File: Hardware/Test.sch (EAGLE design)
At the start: 57 parts, among them IC1 4051N, IC2 TLC5940, IC3 MEGA8-P, T1 BC548, T2 BC548, T3 BC548, T4 BC548, T5 BC548, T6 BC548, T8 BC548, T9 BC548

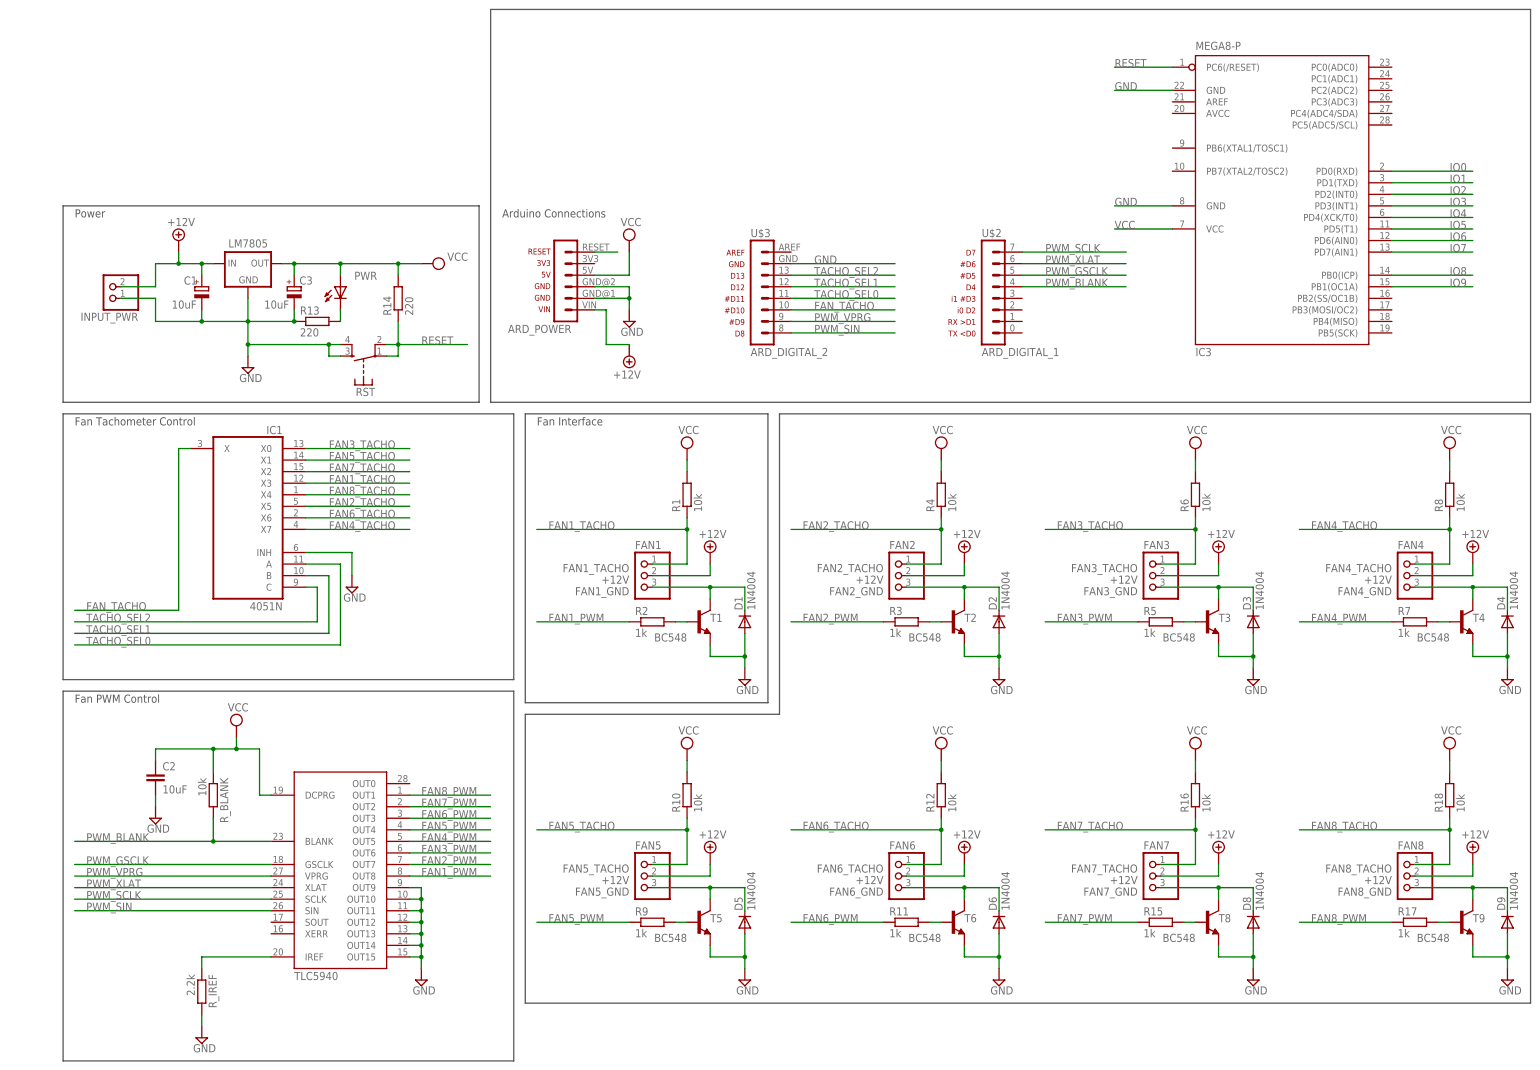
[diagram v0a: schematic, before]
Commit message: Added some test schematics
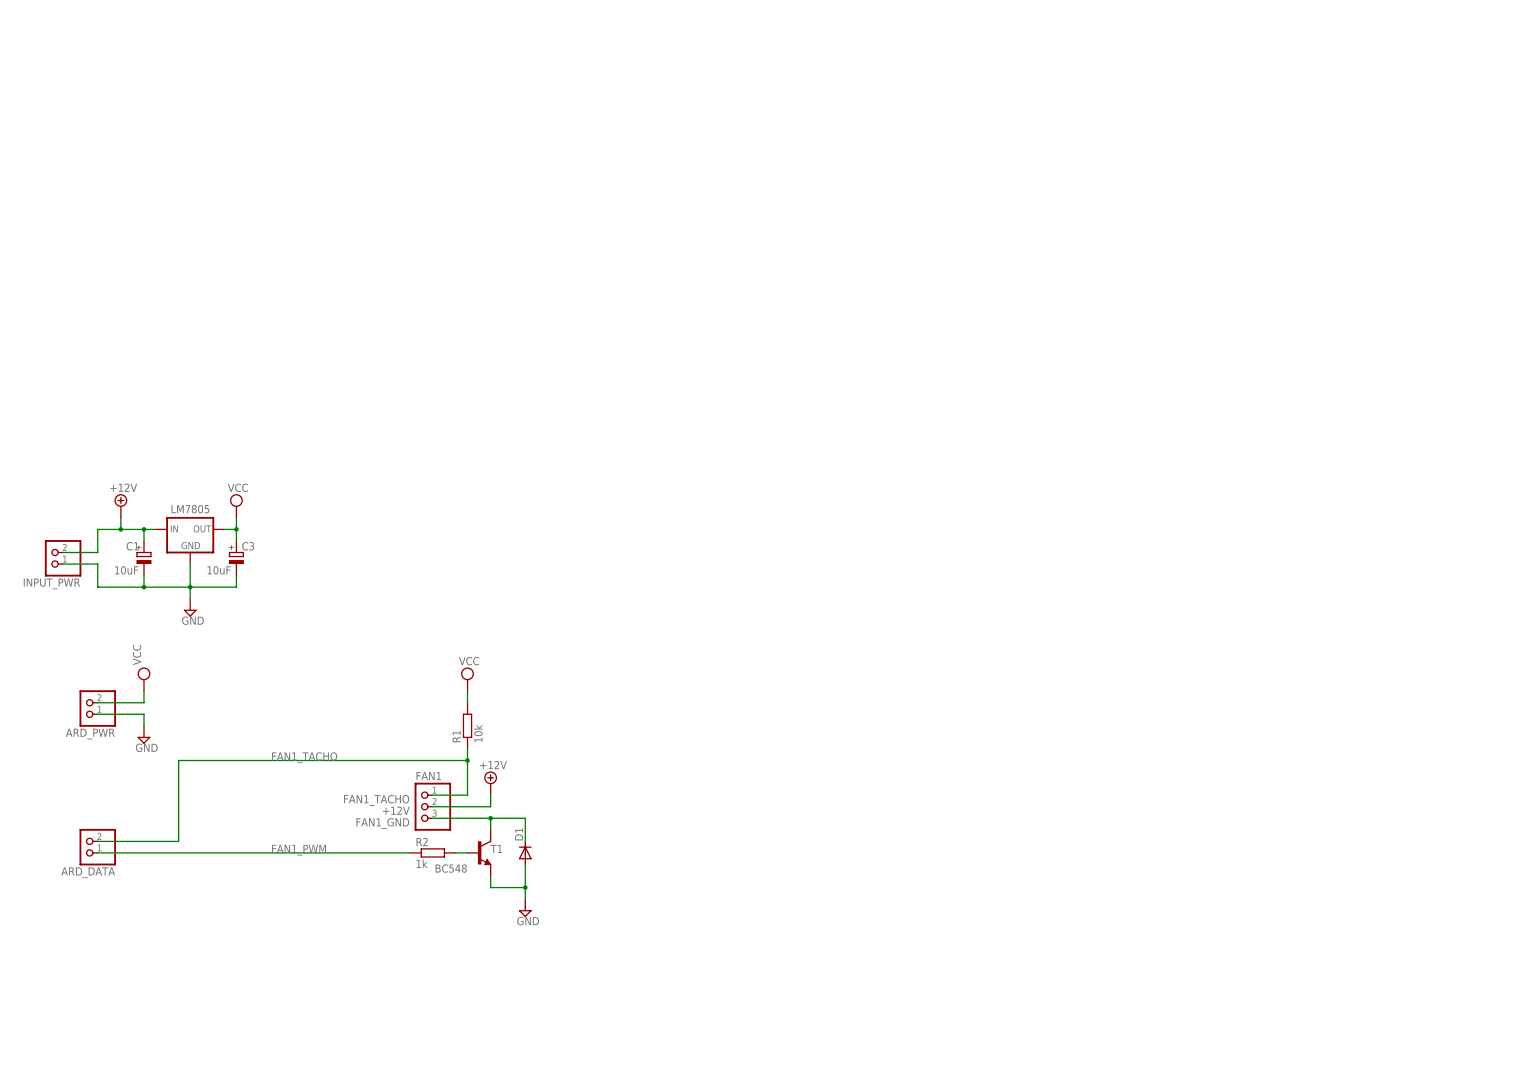
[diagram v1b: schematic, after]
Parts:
- removed C2: 10uF, rcl:C-EU025-025X050
- removed D2, D3, D4, D5, D6, D8, D9: 1N4004, diode:1N4004
- removed FAN2, FAN3, FAN4, FAN5, FAN6, FAN7, FAN8: (no value), pinhead:PINHD-1X3
- removed IC1: 4051N, 40xx:4051N
- removed IC2: TLC5940, EnigmaMon:TLC5940
- removed IC3: MEGA8-P, EnigmaMon:MEGA8-P
- removed PWR: (no value), EnigmaMon:LED3MM
- removed R10, R12, R16, R18, R6, R8, R_BLANK: 10k, rcl:R-EU_0204/7
- removed R11, R15, R17, R3, R5, R7, R9: 1k, rcl:R-EU_0204/7
- removed R13, R14: 220, rcl:R-EU_0204/7
- removed R4: 10k, rcl:R-EU_0207/10
- removed RST: DTS6, EnigmaMon:DTS6
- removed R_IREF: 2.2k, rcl:R-EU_0204/7
- removed T2, T3, T4, T5, T6, T8, T9: BC548, transistor:BC547
- removed U$1: ARD_POWER, EnigmaMon:ARD_POWER
- removed U$2: ARD_DIGITAL_1, EnigmaMon:ARD_DIGITAL_1
- removed U$3: ARD_DIGITAL_2, EnigmaMon:ARD_DIGITAL_2
- added ARD_DATA, ARD_PWR: (no value), EnigmaMon:PINHD-1X2
- D1: value 1N4004 -> (none); device diode:1N4004 -> diode:DIODE-D-7.5
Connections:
- removed net FAN2_GND: D2.C, FAN2.3, T2.C
- removed net FAN2_PWM: IC2G$1.OUT7, R3.1
- removed net FAN2_TACHO: FAN2.1, IC1A.X5, R4.1
- removed net FAN3_GND: D3.C, FAN3.3, T3.C
- removed net FAN3_PWM: IC2G$1.OUT6, R5.1
- removed net FAN3_TACHO: FAN3.1, IC1A.X0, R6.1
- removed net FAN4_GND: D4.C, FAN4.3, T4.C
- removed net FAN4_PWM: IC2G$1.OUT5, R7.1
- removed net FAN4_TACHO: FAN4.1, IC1A.X7, R8.1
- removed net FAN5_GND: D5.C, FAN5.3, T5.C
- removed net FAN5_PWM: IC2G$1.OUT4, R9.1
- removed net FAN5_TACHO: FAN5.1, IC1A.X1, R10.1
- removed net FAN6_GND: D6.C, FAN6.3, T6.C
- removed net FAN6_PWM: IC2G$1.OUT3, R11.1
- removed net FAN6_TACHO: FAN6.1, IC1A.X6, R12.1
- removed net FAN7_GND: D8.C, FAN7.3, T8.C
- removed net FAN7_PWM: IC2G$1.OUT2, R15.1
- removed net FAN7_TACHO: FAN7.1, IC1A.X2, R16.1
- removed net FAN8_GND: D9.C, FAN8.3, T9.C
- removed net FAN8_PWM: IC2G$1.OUT1, R17.1
- removed net FAN8_TACHO: FAN8.1, IC1A.X4, R18.1
- removed net FAN_TACHO: IC1A.X, U$3.10
- removed net IO0: IC3.PD0(RXD)
- removed net IO1: IC3.PD1(TXD)
- removed net IO2: IC3.PD2(INT0)
- removed net IO3: IC3.PD3(INT1)
- removed net IO4: IC3.PD4(XCK/T0)
- removed net IO5: IC3.PD5(T1)
- removed net IO6: IC3.PD6(AIN0)
- removed net IO7: IC3.PD7(AIN1)
- removed net IO8: IC3.PB0(ICP)
- removed net IO9: IC3.PB1(OC1A)
- removed net N$1: R3.2, T2.B
- removed net N$10: IC2G$1.IREF, R_IREF.1
- removed net N$3: R5.2, T3.B
- removed net N$4: R7.2, T4.B
- removed net N$5: R9.2, T5.B
- removed net N$6: R11.2, T6.B
- removed net N$7: PWR.C, R13.2
- removed net N$8: R15.2, T8.B
- removed net N$9: R17.2, T9.B
- removed net PWM_BLANK: IC2G$1.BLANK, R_BLANK.2, U$2.4
- removed net PWM_GSCLK: IC2G$1.GSCLK, U$2.5
- removed net PWM_SCLK: IC2G$1.SCLK, U$2.7
- removed net PWM_SIN: IC2G$1.SIN, U$3.8
- removed net PWM_VPRG: IC2G$1.VPRG, U$3.9
- removed net PWM_XLAT: IC2G$1.XLAT, U$2.6
- removed net RESET: IC3.PC6(/RESET), R14.1, RST.P, RST.P@1, U$1.RESET
- removed net TACHO_SEL0: IC1A.A, U$3.11
- removed net TACHO_SEL1: IC1A.B, U$3.12
- removed net TACHO_SEL2: IC1A.C, U$3.13
- net +12V: no longer FAN2.2, FAN3.2, FAN4.2, FAN5.2, FAN6.2, FAN7.2, FAN8.2, U$1.VIN
- net FAN1_PWM: now also ARD_DATA.1; no longer IC2G$1.OUT8
- net FAN1_TACHO: now also ARD_DATA.2; no longer IC1A.X3
- net GND: now also ARD_PWR.1; no longer C2.2, D2.A, D3.A, D4.A, D5.A, D6.A, D8.A, D9.A, IC1A.INH, IC2G$1.OUT10, IC2G$1.OUT11, IC2G$1.OUT12, IC2G$1.OUT13, IC2G$1.OUT14, IC2G$1.OUT15, IC2G$1.OUT9, IC3.GND, IC3.GND@1, R13.1, RST.S, RST.S@1, R_IREF.2, T2.E, T3.E, T4.E, T5.E, T6.E, T8.E, T9.E, U$1.GND@1, U$1.GND@2, U$3.GND
- net VCC: now also ARD_PWR.2; no longer C2.1, IC2G$1.DCPRG, IC3.VCC@1, PWR.A, R10.2, R12.2, R14.2, R16.2, R18.2, R4.2, R6.2, R8.2, R_BLANK.1, U$1.5V
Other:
- note removed: "Arduino Connections"
- note removed: "Fan Interface"
- note removed: "Fan PWM Control"
- note removed: "Fan Tachometer Control"
- note removed: "Power"
- moved on the sheet: C1, C3, FAN1, INPUT_PWR, LM7805, R1, R2, T1
